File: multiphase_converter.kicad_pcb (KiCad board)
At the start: 4 copper layers, 150 x 235 mm, 219 parts, among them J1 Conn_01x04_Male, J2 1923872, J3 1714955, J4 Conn_01x04_Male, J5 Conn_01x04_Male, J6 Conn_01x02_Male, J7 Conn_01x03_Male, Q1 BC807, Q10 Q_NMOS_GDS, Q2 IPB60R060P7ATMA1, Q3 Q_NMOS_GDS, Q4 Q_NMOS_GDS, Q5 Q_NMOS_GDS, Q6 Q_NMOS_GDS, Q7 Q_NMOS_GDS, Q8 Q_NMOS_GDS, Q9 Q_NMOS_GDS, T1 Wurth_760895751, T2 Wurth_760895751, T3 Wurth_760895751, T4 Wurth_760895751, U1 STM32F334C8Tx, U10 LM317L_SO8, U11 TSV911IDT, U12 74HC4051, U13 TSV911IDT, U14 TSV911IDT, U15 TSV911IDT, U16 TSV911IDT, U2 ADR4525, U3 UCC28180, U4 IR2113S, U5 IR2113S, U6 IR2113S, U7 IR2113S, U8 ADuM260N, U9 AD8551, Y1 ABM3B-16.000MHZ-B2-T

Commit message: Updates to PCB to get ready for manufacture
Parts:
- moved C23 1.55 mm to (56.5, 229.6)
- moved R3 0.76 mm to (82.5, 104.5)
- moved C8 0.75 mm to (84.5, 104.5)
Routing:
- net GNDA: track 73.8 -> 75.5 mm, vias 97 -> 98
- net /Converter Stage/T3_HI: track 80.5 -> 81.5 mm
- net /Converter Stage/T1_HI: track 71.7 -> 72.6 mm
- net Net-(C9-Pad2): track 6.91 -> 7.62 mm
- net VBUS: track 190.6 -> 191.3 mm, vias 125 -> 160
- net /Converter Stage/T4_HI: track 80.3 -> 80.9 mm
- net Net-(D33-Pad3): vias 25 -> 35
- net Net-(D30-Pad3): vias 25 -> 37
- net Net-(D28-Pad3): vias 25 -> 37
- net Net-(C15-Pad2): vias 3 -> 7
- net HRTIM_CHC1: vias 0 -> 1
- net HRTIM_CHA1: vias 0 -> 1
- net /Converter Stage/T3_LO: vias 25 -> 37
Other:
- outline, holes or cut-outs redrawn
- board text added: "CHA1-"
- board text added: "CHB1"
- board text added: "CHC1"
- board text added: "CHD1"
- board text added: "Multiphase Forward Converter Rev1.0"

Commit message: Final design sent out for fabrication
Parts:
- added C61: 1u, Capacitor_SMD:C_0805_2012Metric, F.Cu at (181.7, 32.6)
- C6: value 0.1u -> 1u
- U2: value ADR4525 -> ADR45xx; footprint Package_SO:SOIC-8_3.9x4.9mm_P1.27mm -> Package_SO:SO-8_3.9x4.9mm_P1.27mm
- moved R39 1.87 mm to (92.7, 151.7), turned to 0 degrees
- moved R17 1.81 mm to (91.6, 248.3), turned to 0 degrees
- moved R16 1.78 mm to (91.6, 199.9), turned to 0 degrees
- moved D26 1.75 mm to (98.0, 103.0)
- moved D23 1.75 mm to (97.0, 151.7)
- moved R41 1.74 mm to (93.7, 103.0), turned to 0 degrees
- moved D21 1.72 mm to (95.8, 248.3)
- moved D20 1.71 mm to (95.8, 199.9)
- moved C7 0.15 mm to (179.7, 32.5), turned to 90 degrees
- moved U2 0.12 mm to (174.9, 33.1)
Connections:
- C7 pad 1: GNDD -> +3V3
- C7 pad 2: +3V3 -> GNDD
- D27 pad 1: Net-(D27-Pad1) -> VBUS
- D28 pad 1: Net-(D28-Pad1) -> VBUS
- D29 pad 1: Net-(D29-Pad1) -> /Converter Stage/T3_HI
- D30 pad 1: Net-(D30-Pad1) -> VBUS
- D31 pad 1: Net-(D31-Pad1) -> /Converter Stage/T4_HI
- D32 pad 1: Net-(D32-Pad1) -> /Converter Stage/T2_HI
- D33 pad 1: Net-(D33-Pad1) -> VBUS
- D34 pad 1: Net-(D34-Pad1) -> /Converter Stage/T1_HI
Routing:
- net VCC: track 476.2 -> 163.2 mm
- net Net-(C15-Pad2): track 235.4 -> 239.4 mm
- net Net-(R17-Pad1): track 42.7 -> 46.2 mm
- net Net-(R39-Pad1): track 42.9 -> 46.2 mm
- net GNDA: track 75.5 -> 78.8 mm, vias 98 -> 101
- net Net-(R16-Pad1): track 42.9 -> 45.9 mm
- net Net-(R41-Pad1): track 37.1 -> 39.4 mm
- net +3V3: track 43.8 -> 45.5 mm
- net +5VA: track 284.6 -> 283.3 mm
- net /Converter Stage/T3_HI: track 81.5 -> 80.3 mm
- net I_FB: track 34.4 -> 35.4 mm
- net /Converter Stage/T2_HI: track 80.4 -> 79.4 mm
- net /Converter Stage/T1_HI: track 72.6 -> 71.9 mm
- net /Converter Stage/P3_GATE: track 258.5 -> 259.1 mm
- net VBUS: vias 160 -> 162
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- added copper zone on B.Cu, net VCC
- added copper zone on F.Cu, net VCC

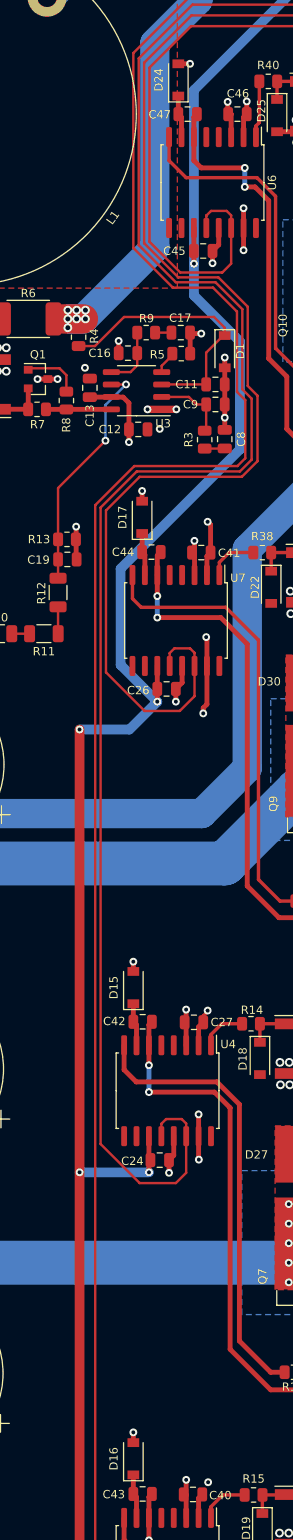
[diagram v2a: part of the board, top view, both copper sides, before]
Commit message: Annotations to schematics, fix bootstrap diodes
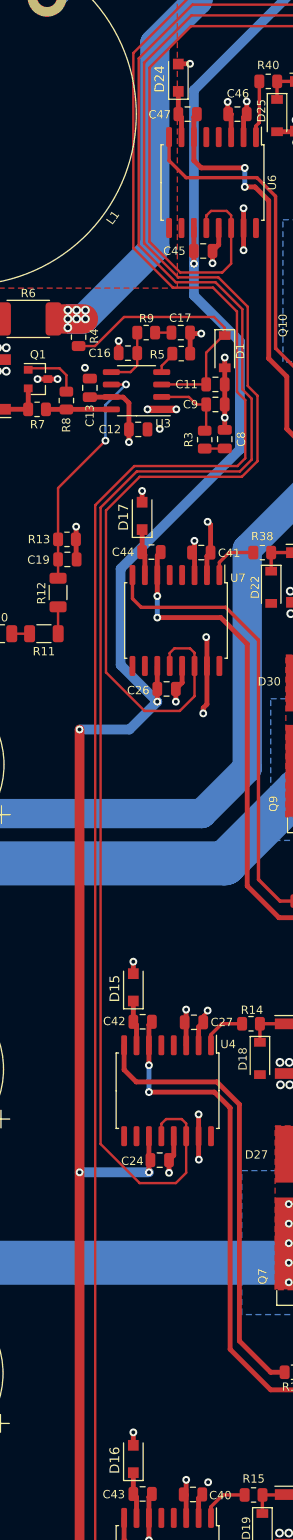
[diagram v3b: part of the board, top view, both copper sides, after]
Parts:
- D15, D16, D17, D24: value D_Schottky -> S1MFL; footprint Diode_SMD:D_SOD-123 -> Diode_SMD:D_SOD-123F
- moved D24 0.23 mm to (79.8, 67.5)
- moved D17 0.15 mm to (76.1, 112.3)
